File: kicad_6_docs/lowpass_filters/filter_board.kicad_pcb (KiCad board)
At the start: 2 copper layers, 167.6 x 101.6 mm, 184 parts, among them J1 comp_dist_board_port, J2 ext_cv_port, J3 env_board_port, J4 lfo_board_port, J5 power_entry, Q1 BCM847, Q10 BCM847, Q11 BCM847, Q12 BCM847, Q13 BCM847, Q14 BCM847, Q15 BCM847, Q16 BCM847, Q17 MMBT3906, Q18 MMBT3904, Q2 BCM847, Q3 BCM847, Q4 BCM847, Q5 BCM847, Q6 BCM847, Q7 BCM847, Q8 MMBT3906, Q9 MMBT3904, U1 TL072, U2 TL072, U3 SSI2164, U4 TL072, U5 TL072, U6 TL072, U7 TL072

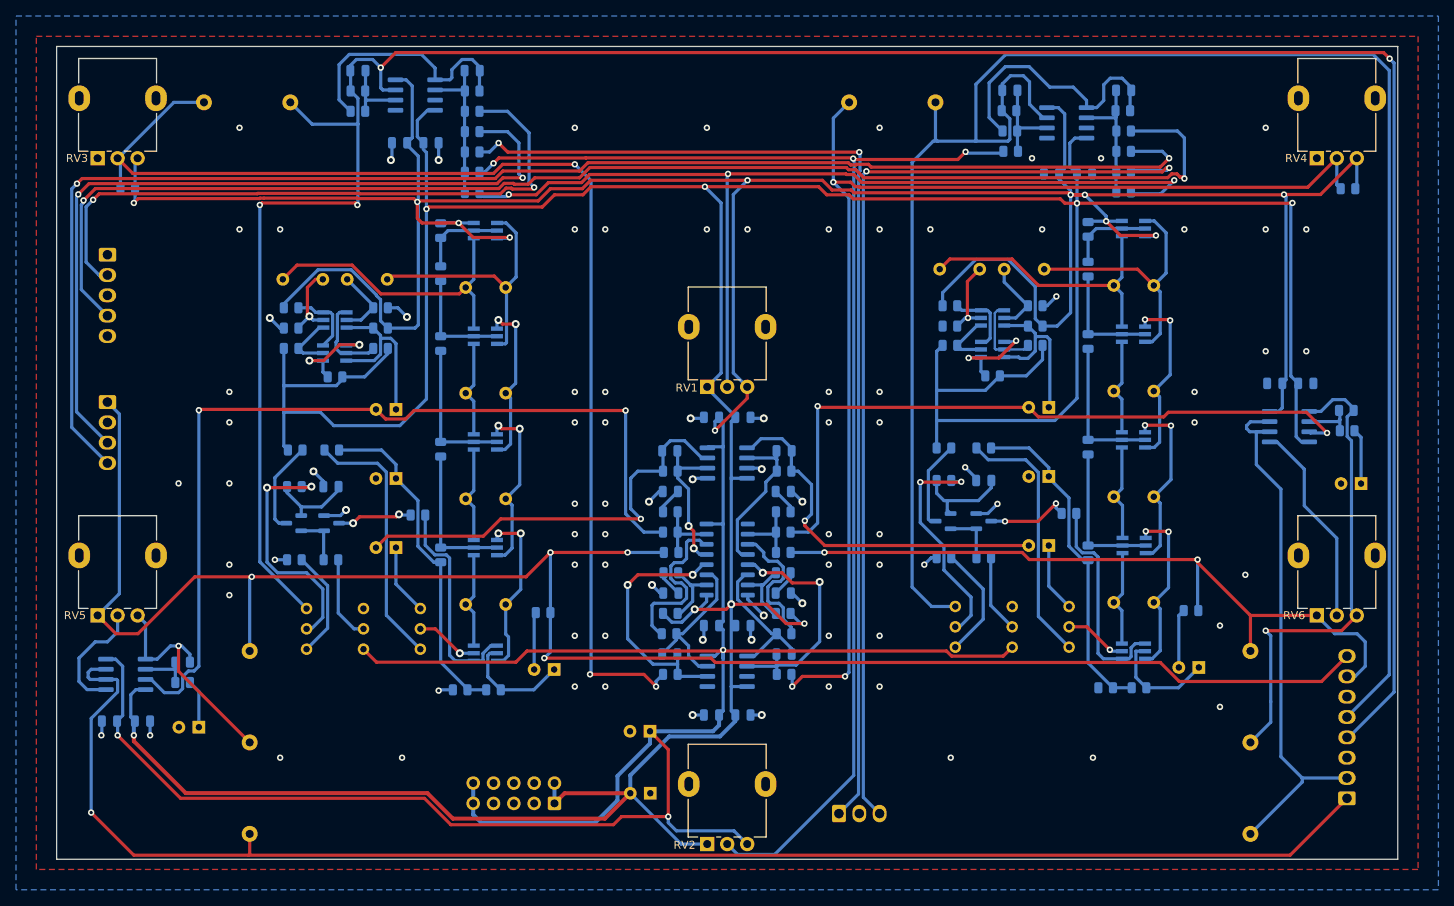
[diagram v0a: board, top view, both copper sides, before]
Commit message: Tweak some filter board values
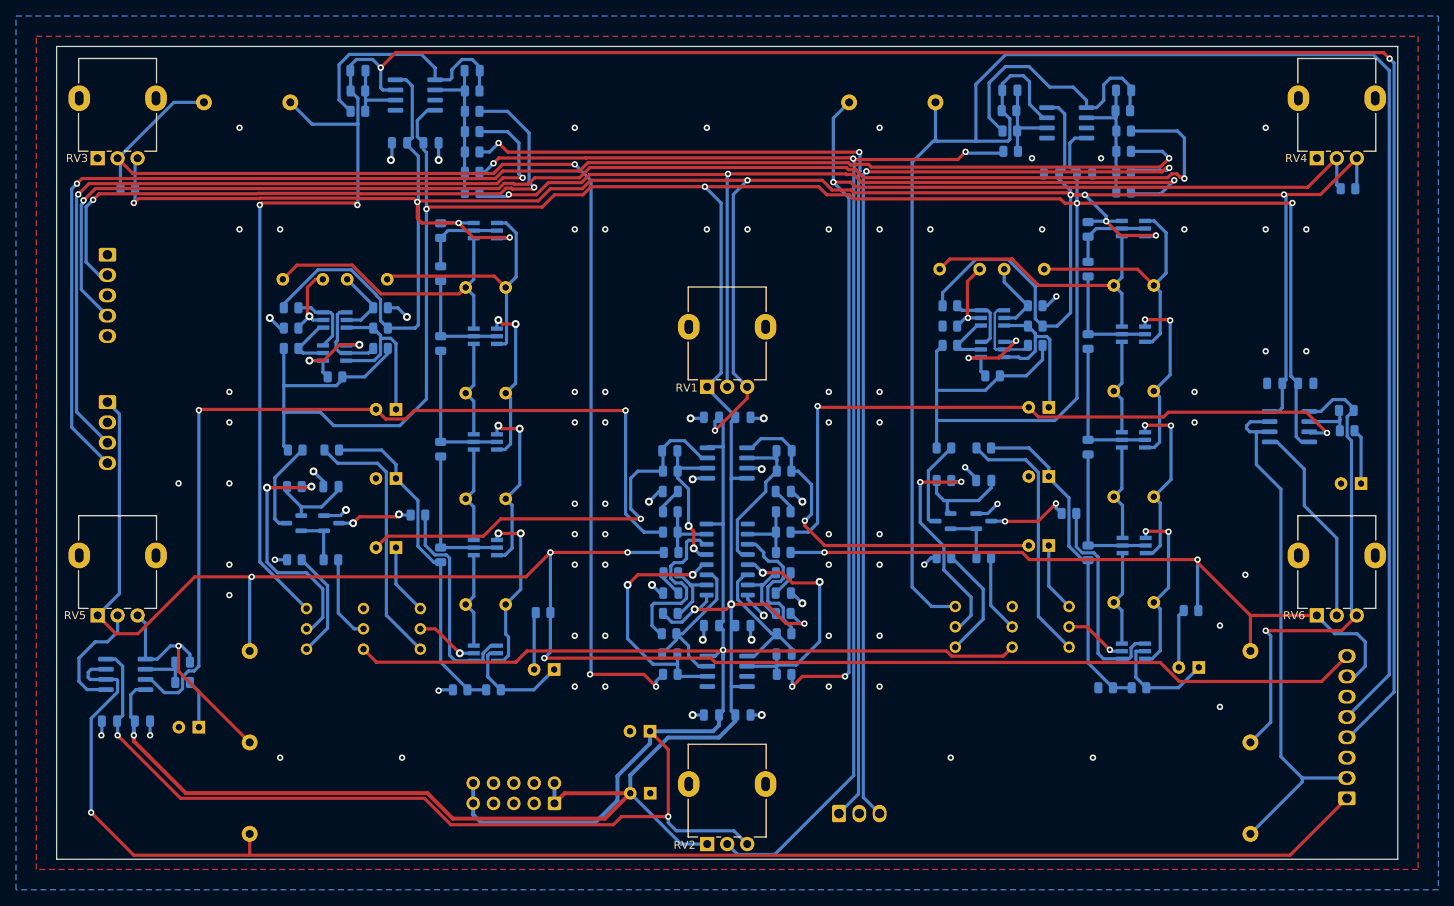
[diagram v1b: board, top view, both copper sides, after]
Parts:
- C21, C9: value 10u -> DNF
- R15, R6: value 100k -> 3k9
- R24, R47: value 20k -> DNF
- R33, R56: value 10k -> 33k
- R38, R61: value ??? -> 100k
- R39, R62: value 1k -> 220
- R65, R73: value 200k -> 33k
